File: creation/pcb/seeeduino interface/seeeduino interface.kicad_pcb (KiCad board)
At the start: 2 copper layers, 31 x 23 mm, 12 parts

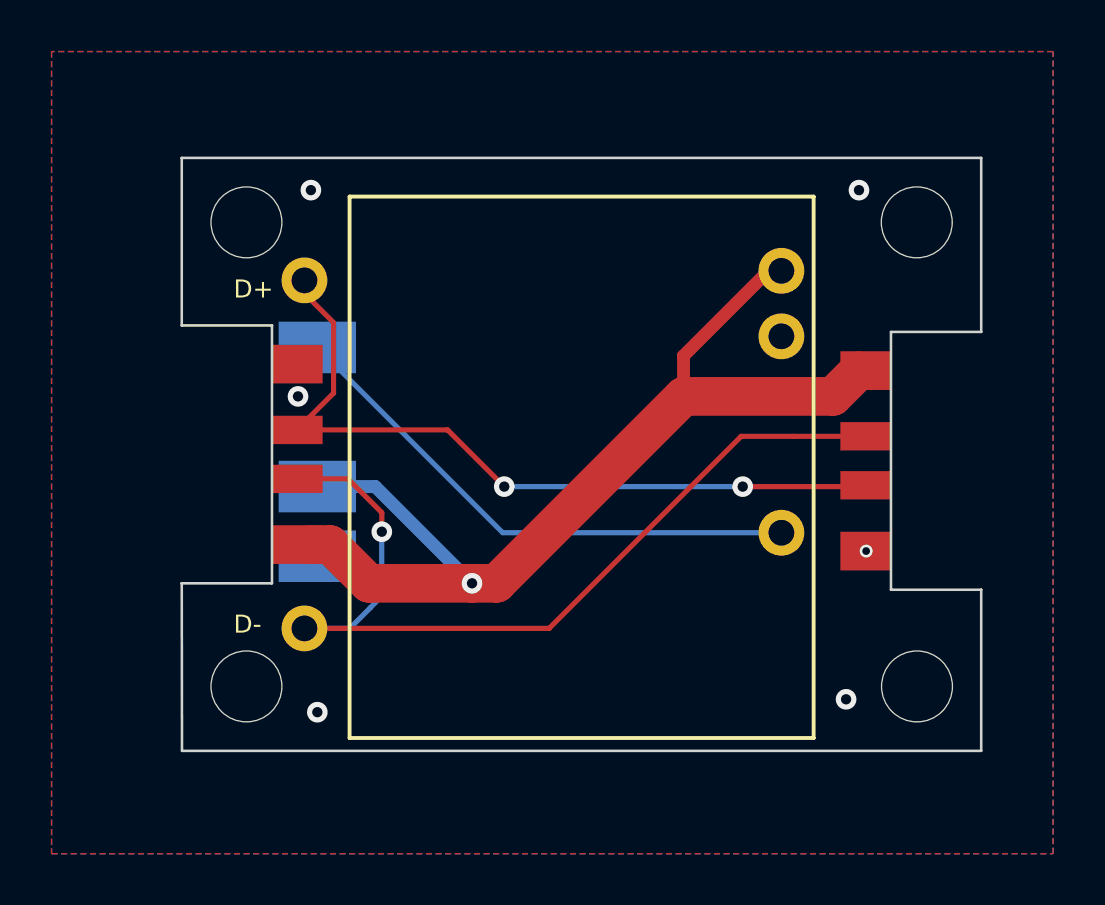
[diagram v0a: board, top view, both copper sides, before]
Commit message: Updated arduino pcb. Ota updates now block rendering with extra indicator pixel.
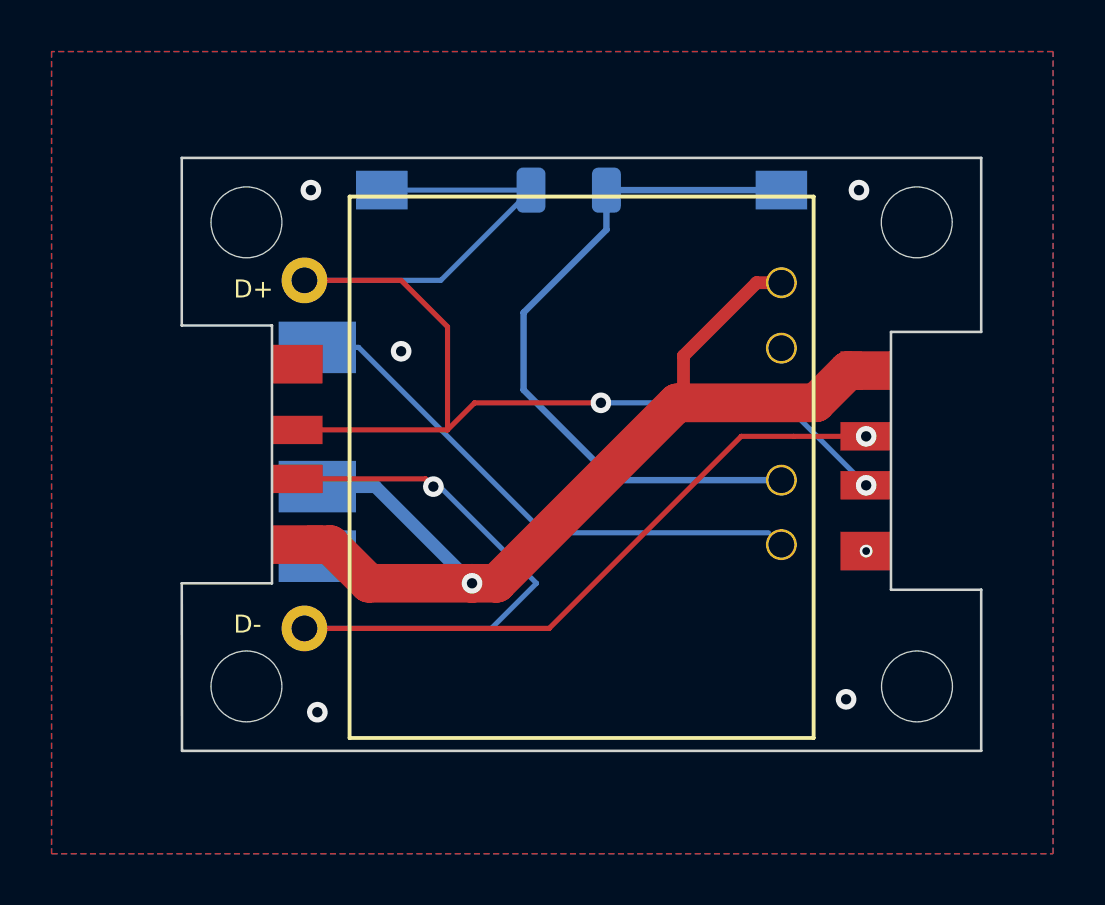
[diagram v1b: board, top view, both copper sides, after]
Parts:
- added ?: , , F.Cu at (123.2, 96.0)
- added ?: , , B.Cu at (107.8, 84.8)
- added ?: , , B.Cu at (123.2, 84.8)
- added REF**: R_1206_3216Metric, Resistor_SMD:R_1206_3216Metric, B.Cu at (115.0, 84.8)
- moved A1 0.46 mm to (123.2, 96.0)
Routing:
- net R1: track 0.00 -> 27.3 mm
- net DATA+: track 30.1 -> 50.7 mm
- net DATA-: track 34.2 -> 44.3 mm, vias 1 -> 2
